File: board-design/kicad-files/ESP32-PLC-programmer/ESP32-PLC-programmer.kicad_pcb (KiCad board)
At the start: 2 copper layers, 38.1 x 50.8 mm, 28 parts, among them J1 302-S101, J2 0473460001, J3 302-S101, U1 TPS62060DSGR, U2 FT231XS

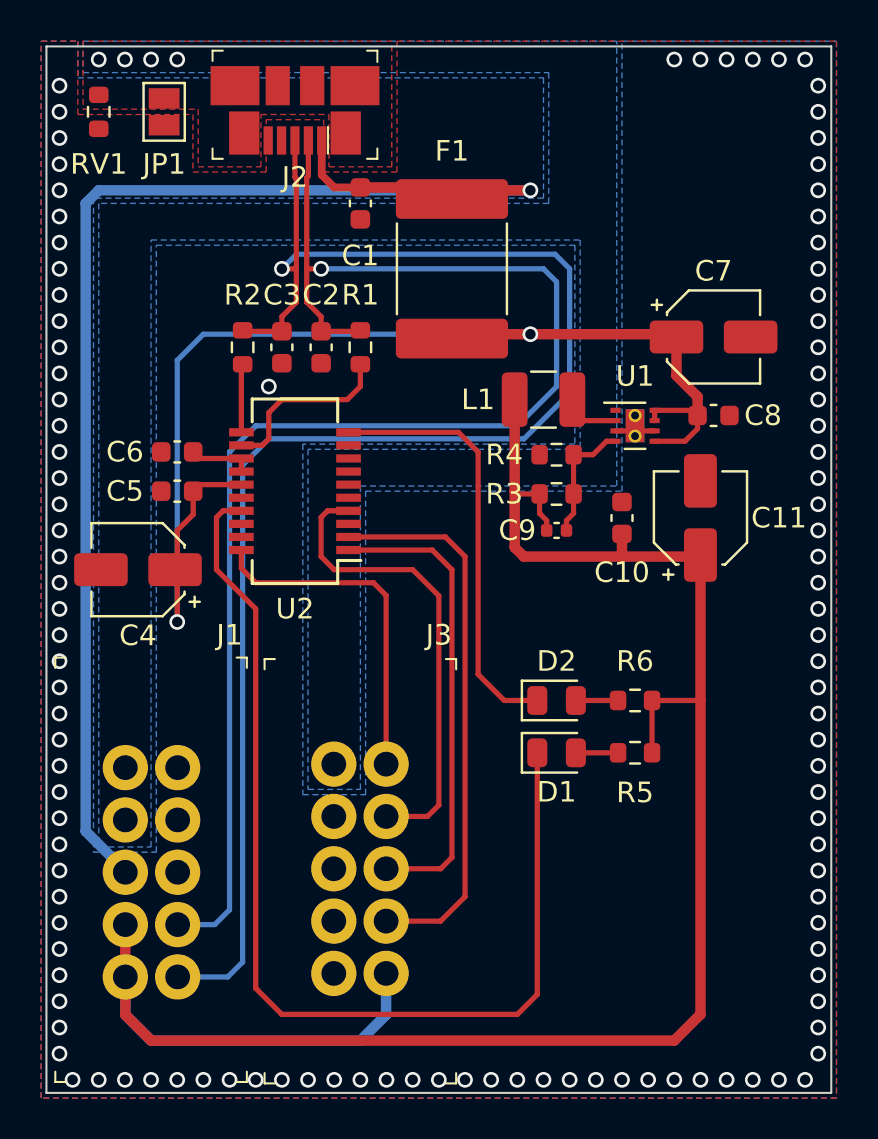
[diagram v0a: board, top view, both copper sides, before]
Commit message: [UPDATE]
Finished ESP32 and ESP32-programmer board designs (few corrections to be made when manufacturer is chosen - design rules).

Signed-off-by: Nicolae-Andrei Vasile <vasilenicolaeandrei@gmail.com>
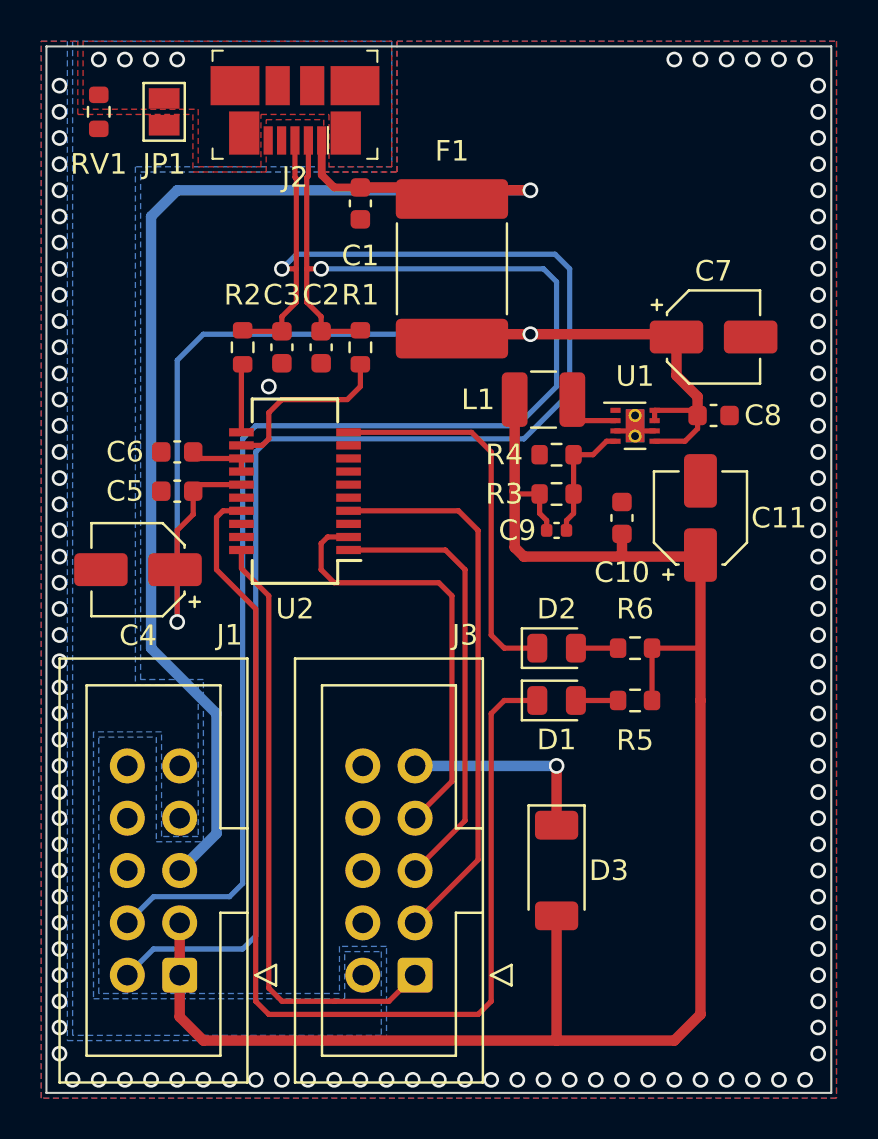
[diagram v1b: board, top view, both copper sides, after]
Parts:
- added D3: 30V/2A/0.7V (RB068LAM-30TFTR), Diode_SMD:D_SOD-128, F.Cu at (151.8, 103.5)
- J1, J3: footprint digikey-footprints:PinHeader_2x5_P2.54mm_Drill1.2mm -> Connector_IDC:IDC-Header_2x05_P2.54mm_Vertical
- moved J3 10.3 mm to (144.9, 108.6), turned to 180 degrees
- moved J1 2.64 mm to (133.5, 108.6), turned to 180 degrees
- moved D1 2.54 mm to (151.8, 95.2)
- moved D2 2.54 mm to (151.8, 92.7)
- moved R5 2.54 mm to (155.6, 95.2)
- moved R6 2.54 mm to (155.6, 92.7)
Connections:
- J3 pad 9: +3V3 -> Net-(D3-K)
- U1 pad 9: GND -> (no net)
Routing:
- net +3V3: track 98.8 -> 84.8 mm
- net Net-(U2-TXD): track 16.7 -> 29.7 mm
- net Net-(D3-K): track 0.00 -> 9.75 mm, vias 0 -> 1
- net Net-(U2-~{RTS}): track 26.9 -> 21.1 mm
- net Net-(U2-RXD): track 22.8 -> 27.0 mm
- net Net-(D1-K): track 51.3 -> 54.1 mm
- net /VBUS: track 67.6 -> 65.2 mm
- net Net-(D2-K): track 20.9 -> 18.7 mm
- net /D-: track 71.2 -> 73.3 mm
- net /D+: track 77.7 -> 79.7 mm
- net Net-(U2-~{DTR}): track 22.8 -> 21.7 mm
